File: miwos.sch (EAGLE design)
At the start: 46 parts

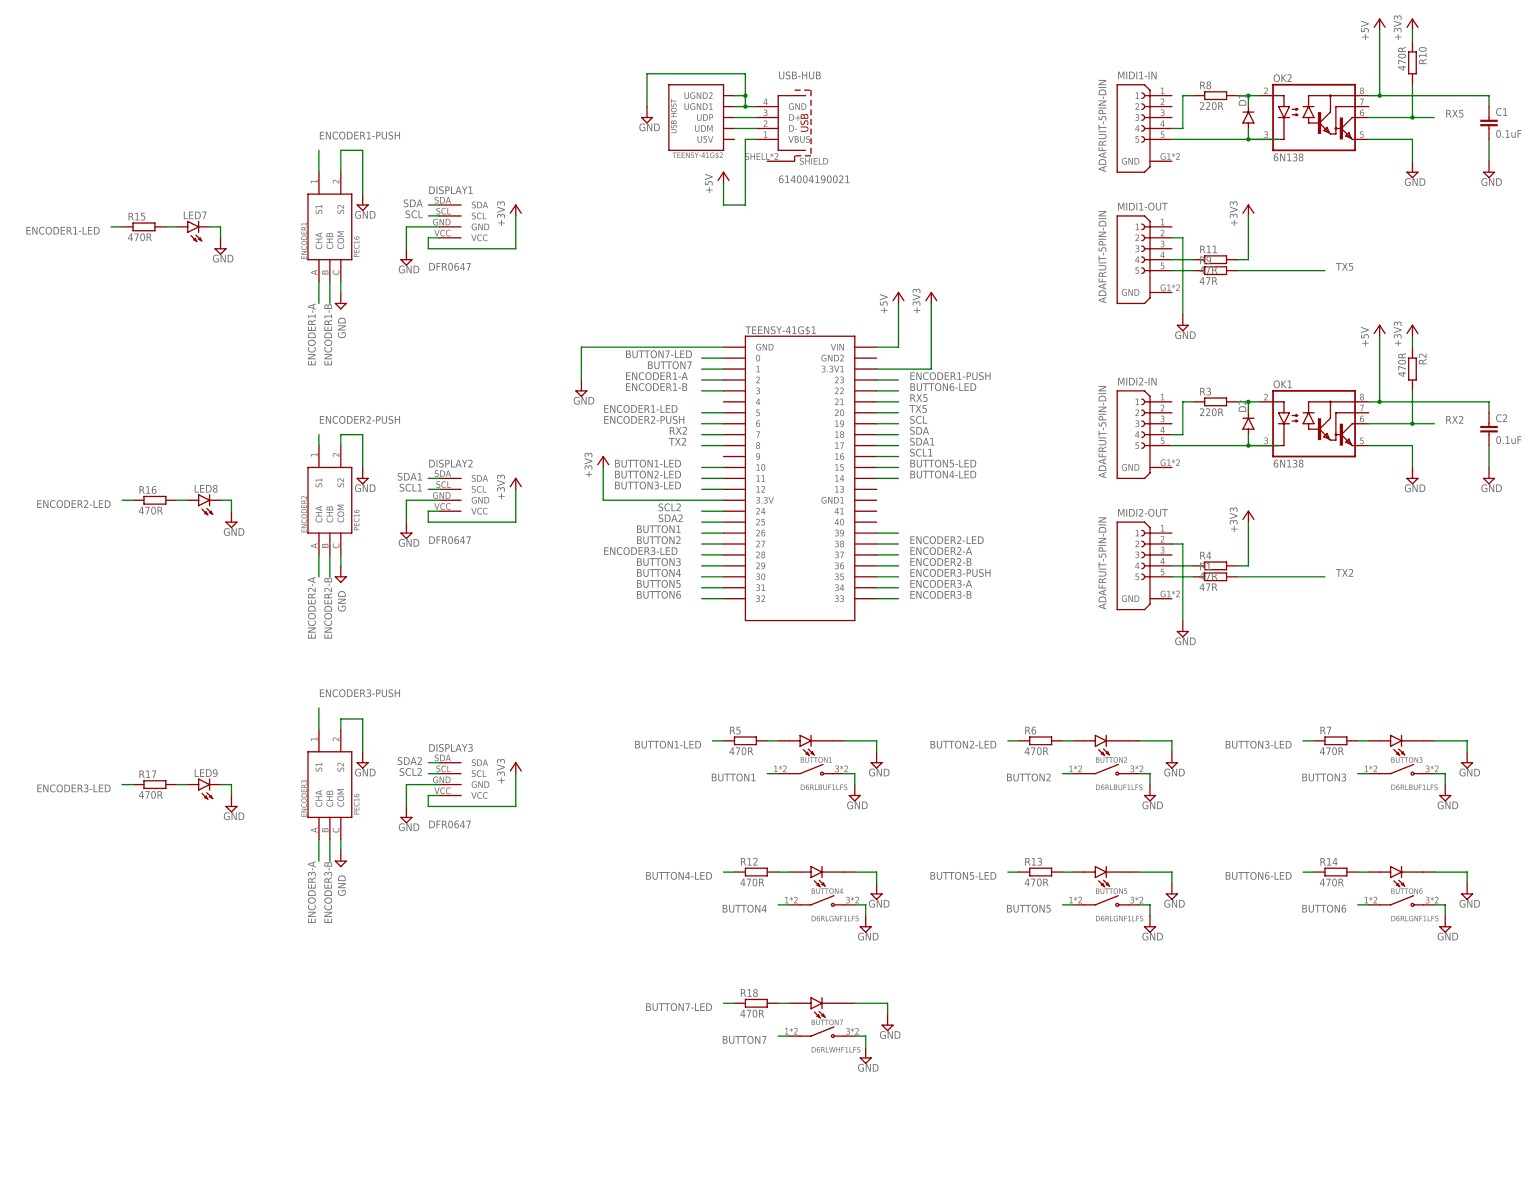
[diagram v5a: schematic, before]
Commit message: Use non-illuminated buttons, add mounting holes
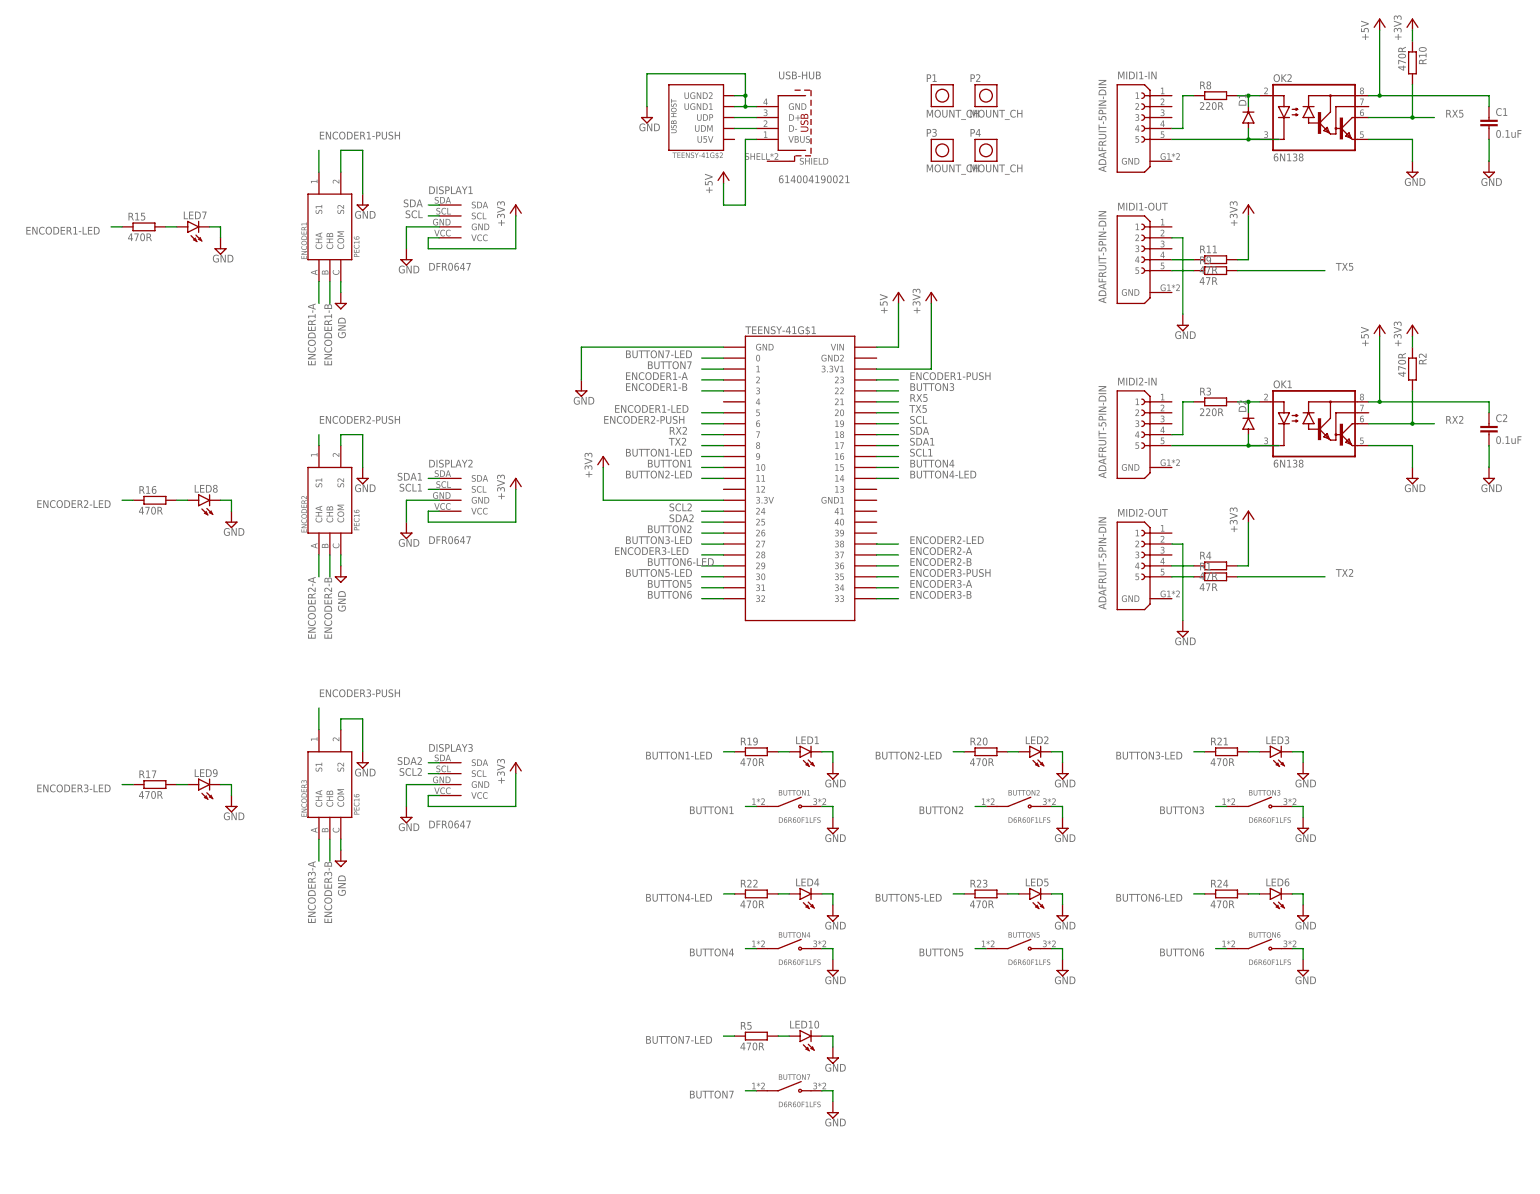
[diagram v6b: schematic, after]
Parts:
- removed R12, R13, R14, R18, R6, R7: 470R, rcl:R-EU_R0603
- added LED1, LED10, LED2, LED3, LED4, LED5, LED6: (no value), led:LED3MM
- added P1, P2, P3, P4: MOUNT_CH, sol_pin:MOUNT_CH
- added R19, R20, R21, R22, R23, R24: 470R, rcl:R-EU_R0603
- BUTTON1, BUTTON2, BUTTON3: value D6RLBUF1LFS -> D6R60F1LFS; device D6RL:D6RLBUF1LFS -> D6R:D6R60F1LFS
- BUTTON4, BUTTON5, BUTTON6: value D6RLGNF1LFS -> D6R60F1LFS; device D6RL:D6RLGNF1LFS -> D6R:D6R60F1LFS
- BUTTON7: value D6RLWHF1LFS -> D6R60F1LFS; device D6RL:D6RLWHF1LFS -> D6R:D6R60F1LFS
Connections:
- removed net N$1: TEENSY-41G$1.39
- removed net N$13: BUTTON4.LED, R12.2
- removed net N$14: BUTTON1.LED, R5.2
- removed net N$15: BUTTON6.LED, R14.2
- removed net N$23: BUTTON5.LED, R13.2
- removed net N$6: BUTTON2.LED, R6.2
- removed net N$7: BUTTON7.LED, R18.2
- new net N$25: LED1.A, R19.2
- new net N$27: LED2.A, R20.2
- new net N$29: LED3.A, R21.2
- new net N$31: LED4.A, R22.2
- new net N$33: LED5.A, R23.2
- new net N$35: LED6.A, R24.2
- net BUTTON1: now also TEENSY-41G$1.10; no longer TEENSY-41G$1.26
- net BUTTON1-LED: now also R19.1, TEENSY-41G$1.9; no longer R5.1, TEENSY-41G$1.10
- net BUTTON2: now also TEENSY-41G$1.26; no longer TEENSY-41G$1.27
- net BUTTON2-LED: now also R20.1; no longer R6.1
- net BUTTON3: now also TEENSY-41G$1.22; no longer TEENSY-41G$1.29
- net BUTTON3-LED: now also R21.1, TEENSY-41G$1.27; no longer R7.1, TEENSY-41G$1.12
- net BUTTON4: now also TEENSY-41G$1.15; no longer TEENSY-41G$1.30
- net BUTTON4-LED: now also R22.1; no longer R12.1
- net BUTTON5-LED: now also R23.1, TEENSY-41G$1.30; no longer R13.1, TEENSY-41G$1.15
- net BUTTON6-LED: now also R24.1, TEENSY-41G$1.29; no longer R14.1, TEENSY-41G$1.22
- net BUTTON7-LED: now also R5.1; no longer R18.1
- net GND: now also LED1.C, LED10.C, LED2.C, LED3.C, LED4.C, LED5.C, LED6.C; no longer BUTTON1.COM-LED, BUTTON2.COM-LED, BUTTON3.COM-LED, BUTTON4.COM-LED, BUTTON5.COM-LED, BUTTON6.COM-LED, BUTTON7.COM-LED
- net N$5: now also LED10.A, R5.2; no longer BUTTON3.LED, R7.2
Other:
- moved on the sheet: R5

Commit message: Various changes
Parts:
- removed LED7, LED8, LED9: (no value), led:LED3MM
- removed R15, R16, R17: 470R, rcl:R-EU_R0603
- ENCODER2: value PEC16 -> PEC11R-4215F-S0024; device PEC16:PEC16 -> PEC11R-4215F-S0024:PEC11R-4215F-S0024
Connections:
- removed net ENCODER1-LED: R15.1, TEENSY-41G$1.5
- removed net ENCODER2-LED: R16.1, TEENSY-41G$1.38
- removed net ENCODER3-LED: R17.1, TEENSY-41G$1.28
- removed net N$20: LED8.A, R16.2
- removed net N$22: LED9.A, R17.2
- removed net N$4: LED7.A, R15.2
- net ENCODER2-A: now also ENCODER2.A; no longer ENCODER2.CHA
- net ENCODER2-B: now also ENCODER2.B; no longer ENCODER2.CHB
- net ENCODER2-PUSH: now also ENCODER2.1; no longer ENCODER2.S1
- net GND: now also ENCODER2.2; no longer ENCODER2.S2, LED7.C, LED8.C, LED9.C

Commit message: Use TRS midi
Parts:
- removed P1, P2, P3, P4: MOUNT_CH, sol_pin:MOUNT_CH
- ENCODER2: value PEC11R-4215F-S0024 -> PEC16; device PEC11R-4215F-S0024:PEC11R-4215F-S0024 -> PEC16:PEC16
- MIDI1-IN, MIDI1-OUT, MIDI2-IN, MIDI2-OUT: value ADAFRUIT-5PIN-DIN -> 35RASMT2BHNTRX; device adafruit-5pin-din:ADAFRUIT-5PIN-DIN -> 35RASMT2BHNTRX:35RASMT2BHNTRX
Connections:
- net ENCODER2-A: now also ENCODER2.CHA; no longer ENCODER2.A
- net ENCODER2-B: now also ENCODER2.CHB; no longer ENCODER2.B
- net ENCODER2-PUSH: now also ENCODER2.S1; no longer ENCODER2.1
- net GND: now also ENCODER2.S2, MIDI1-OUT.5, MIDI2-OUT.5; no longer ENCODER2.2, MIDI1-OUT.2, MIDI2-OUT.2
- net N$10: now also MIDI1-IN.1; no longer MIDI1-IN.4
- net N$11: now also MIDI1-OUT.4; no longer MIDI1-OUT.5
- net N$12: now also MIDI1-OUT.1; no longer MIDI1-OUT.4
- net N$17: now also MIDI2-IN.4; no longer MIDI2-IN.5
- net N$18: now also MIDI2-IN.1; no longer MIDI2-IN.4
- net N$19: now also MIDI2-OUT.4; no longer MIDI2-OUT.5
- net N$21: now also MIDI2-OUT.1; no longer MIDI2-OUT.4
- net N$9: now also MIDI1-IN.4; no longer MIDI1-IN.5
